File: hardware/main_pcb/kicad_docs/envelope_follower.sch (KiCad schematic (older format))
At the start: 21 parts, among them SW1 env_invert, U6 TL072, U7 TL072

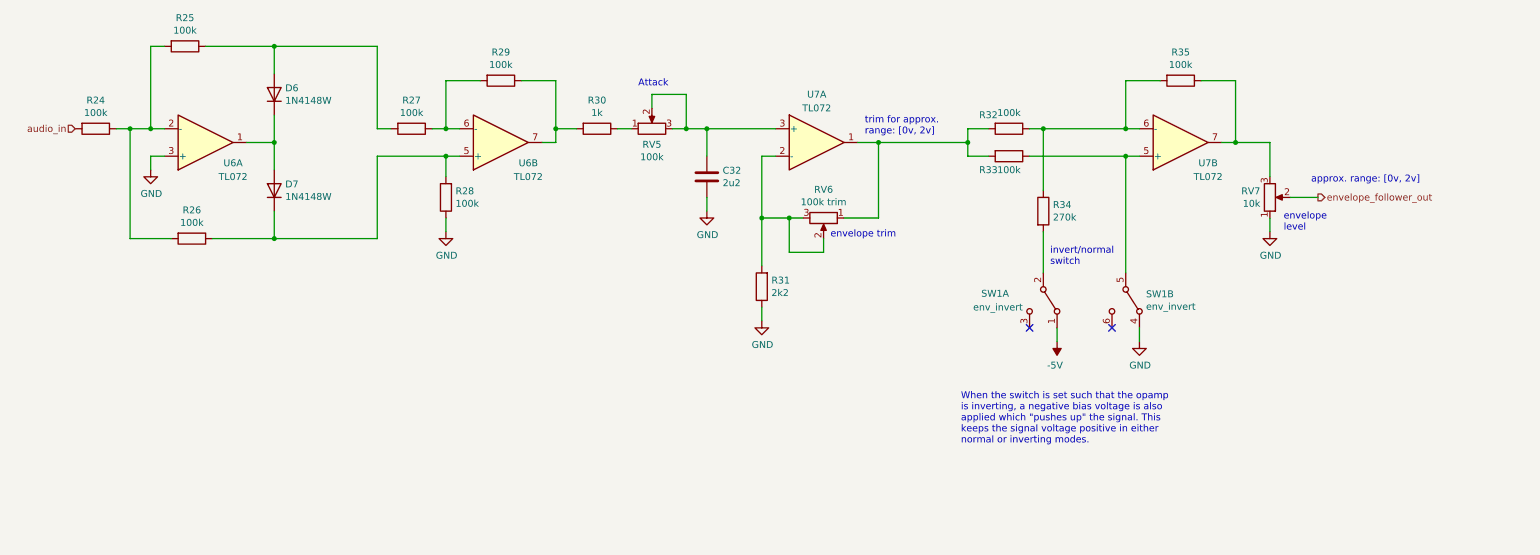
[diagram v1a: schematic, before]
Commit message: center envelope follower around +1v, tidy up
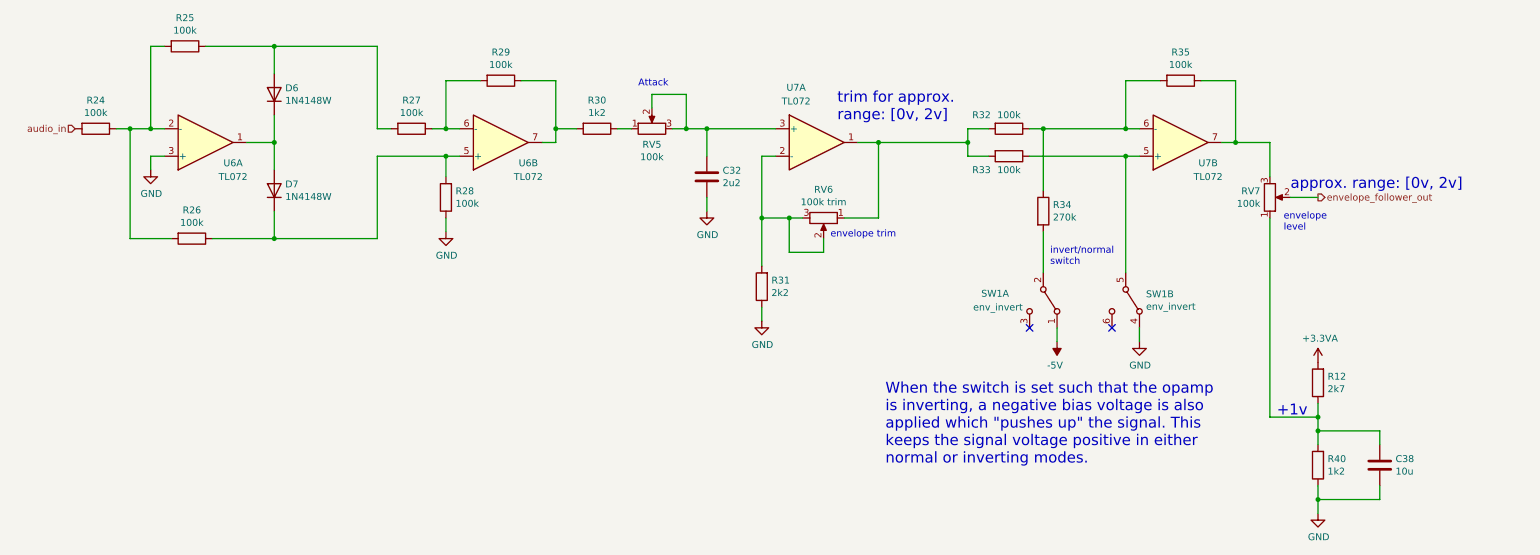
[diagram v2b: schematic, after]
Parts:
- added C38: 10u, Capacitor_SMD:C_0805_2012Metric, symbol Device:C
- added R12: 2k7, Resistor_SMD:R_0805_2012Metric, symbol Device:R
- added R40: 1k2, Resistor_SMD:R_0805_2012Metric, symbol Device:R
- R30: value 1k -> 1k2
- RV7: value 10k -> 100k
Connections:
- net GND: now also C38.2, R40.1; no longer RV7.1
- new net: C38.1, R12.1, R40.2, RV7.1
- new net +3.3VA: R12.2
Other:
- note added: "+1v"
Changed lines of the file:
@@
 Sheet 6 8
 Title "Whooshy Sound Filter Pedal"
-Date "2021-06-29"
-Rev "0"
+Date "2021-08-05"
+Rev "0.1"
 Comp ""
 Comment1 "creativecommons.org/licenses/by/4.0/"
@@
 P 4750 3100
 F 0 "R30" V 4543 3100 50  0000 C CNN
-F 1 "1k" V 4634 3100 50  0000 C CNN
+F 1 "1k2" V 4634 3100 50  0000 C CNN
 F 2 "Resistor_SMD:R_0805_2012Metric" V 4680 3100 50  0001 C CNN
 F 3 "~" H 4750 3100 50  0001 C CNN
@@
 U 1 1 60DCC5FC
 P 6350 3200
-F 0 "U7" H 6350 3550 50  0000 C CNN
-F 1 "TL072" H 6350 3450 50  0000 C CNN
+F 0 "U7" H 6200 3600 50  0000 C CNN
+F 1 "TL072" H 6200 3500 50  0000 C CNN
 F 2 "Package_SO:SOIC-8_3.9x4.9mm_P1.27mm" H 6350 3200 50  0001 C CNN
 F 3 "http://www.ti.com/lit/ds/symlink/tl071.pdf" H 6350 3200 50  0001 C CNN
@@
 U 1 1 60E16310
 P 7750 3100
-F 0 "R32" V 7650 2950 50  0000 C CNN
-F 1 "100k" V 7634 3100 50  0000 C CNN
+F 0 "R32" V 7650 2900 50  0000 C CNN
+F 1 "100k" V 7650 3100 50  0000 C CNN
 F 2 "Resistor_SMD:R_0805_2012Metric" V 7680 3100 50  0001 C CNN
 F 3 "~" H 7750 3100 50  0001 C CNN
@@
 U 1 1 60E17797
 P 7750 3300
-F 0 "R33" V 7850 3150 50  0000 C CNN
+F 0 "R33" V 7850 3100 50  0000 C CNN
 F 1 "100k" V 7850 3300 50  0000 C CNN
 F 2 "Resistor_SMD:R_0805_2012Metric" V 7680 3300 50  0001 C CNN
@@
 	6800 3200 7450 3200
 Connection ~ 6800 3200
-Text Notes 6700 3150 0    50   ~ 0
+Text Notes 6500 3050 0    79   ~ 0
 trim for approx.\nrange: [0v, 2v]
 Wire Wire Line
@@
 Wire Wire Line
 	9400 2750 9400 3200
-Text Notes 7400 5400 0    50   ~ 0
+Text Notes 6850 5550 0    79   ~ 0
 When the switch is set such that the opamp\nis inverting, a negative bias voltage is also \napplied which "pushes up" the signal. This\nkeeps the signal voltage positive in either\nnormal or inverting modes.
-Wire Wire Line
-	9650 3850 9650 3750
 $Comp
 L power:GND #PWR051
 U 1 1 60E6CC94
-P 9650 3850
-F 0 "#PWR051" H 9650 3600 50  0001 C CNN
-F 1 "GND" H 9655 3677 50  0000 C CNN
-F 2 "" H 9650 3850 50  0001 C CNN
-F 3 "" H 9650 3850 50  0001 C CNN
-	1    9650 3850
+P 10000 5900
+F 0 "#PWR051" H 10000 5650 50  0001 C CNN
+F 1 "GND" H 10005 5727 50  0000 C CNN
+F 2 "" H 10000 5900 50  0001 C CNN
+F 3 "" H 10000 5900 50  0001 C CNN
+	1    10000 5900
 	1    0    0    -1
 $EndComp
@@
 P 9650 3600
 F 0 "RV7" H 9580 3554 50  0000 R CNN
-F 1 "10k" H 9580 3645 50  0000 R CNN
+F 1 "100k" H 9580 3645 50  0000 R CNN
 F 2 "Potentiometer_THT:Potentiometer_Alpha_RD901F-40-00D_Single_Vertical" H 9650 3600 50  0001 C CNN
 F 3 "~" H 9650 3600 50  0001 C CNN
@@
 Wire Wire Line
 	9800 3600 10000 3600
-Text Notes 9950 3500 0    50   ~ 0
+Text Notes 9800 3550 0    79   ~ 0
 approx. range: [0v, 2v]
 Text HLabel 10000 3600 2    50   Output ~ 0
@@
 	8700 4650 8700 4550
 NoConn ~ 8500 4550
+$Comp
+L Device:R R40
+U 1 1 60F4FA0F
+P 10000 5550
+F 0 "R40" H 9930 5504 50  0000 R CNN
+F 1 "1k2" H 9930 5595 50  0000 R CNN
+F 2 "Resistor_SMD:R_0805_2012Metric" V 9930 5550 50  0001 C CNN
+F 3 "~" H 10000 5550 50  0001 C CNN
+	1    10000 5550
+	-1   0    0    1
+$EndComp
+$Comp
+L Device:R R12
+U 1 1 60F54D90
+P 10000 4950
+F 0 "R12" H 9930 4904 50  0000 R CNN
+F 1 "2k7" H 9930 4995 50  0000 R CNN
+F 2 "Resistor_SMD:R_0805_2012Metric" V 9930 4950 50  0001 C CNN
+F 3 "~" H 10000 4950 50  0001 C CNN
+	1    10000 4950
+	-1   0    0    1
+$EndComp
+$Comp
+L Device:C C38
+U 1 1 60F564CD
+P 10450 5550
+F 0 "C38" H 10565 5596 50  0000 L CNN
+F 1 "10u" H 10565 5505 50  0000 L CNN
+F 2 "Capacitor_SMD:C_0805_2012Metric" H 10488 5400 50  0001 C CNN
+F 3 "~" H 10450 5550 50  0001 C CNN
+	1    10450 5550
+	1    0    0    -1
+$EndComp
+Wire Wire Line
+	10000 5700 10000 5800
+Wire Wire Line
+	10000 5800 10450 5800
+Wire Wire Line
+	10450 5800 10450 5700
+Connection ~ 10000 5800
+Wire Wire Line
+	10000 5800 10000 5900
+Wire Wire Line
+	10450 5400 10450 5300
+Wire Wire Line
+	10450 5300 10000 5300
+Wire Wire Line
+	10000 5300 10000 5400
+Wire Wire Line
+	10000 5300 10000 5200
+Connection ~ 10000 5300
+Wire Wire Line
+	9650 5200 10000 5200
+Wire Wire Line
+	9650 3750 9650 5200
+Connection ~ 10000 5200
+Wire Wire Line
+	10000 5200 10000 5100
+$Comp
+L power:+3.3VA #PWR038
+U 1 1 60F6E10C
+P 10000 4800
+F 0 "#PWR038" H 10000 4650 50  0001 C CNN
+F 1 "+3.3VA" H 10015 4973 50  0000 C CNN
+F 2 "" H 10000 4800 50  0001 C CNN
+F 3 "" H 10000 4800 50  0001 C CNN
+	1    10000 4800
+	1    0    0    -1
+$EndComp
+Text Notes 9700 5200 0    79   ~ 0
++1v
 $EndSCHEMATC
